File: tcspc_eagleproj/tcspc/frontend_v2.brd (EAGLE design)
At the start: 25.4 x 25.4 mm, 11 parts, among them U1 AD8465, X1 SMA

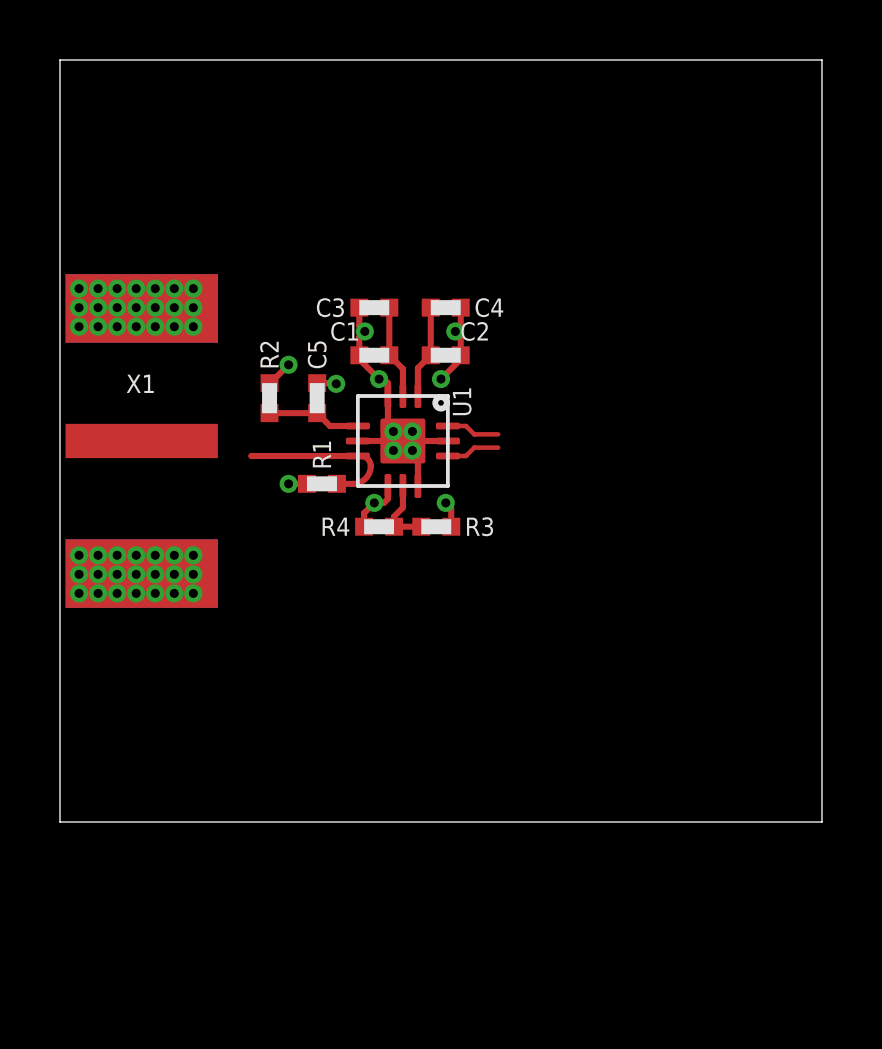
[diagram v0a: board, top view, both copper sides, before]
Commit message: turned the frontend into a useful designblock, ready to be pased all over the tcspc board
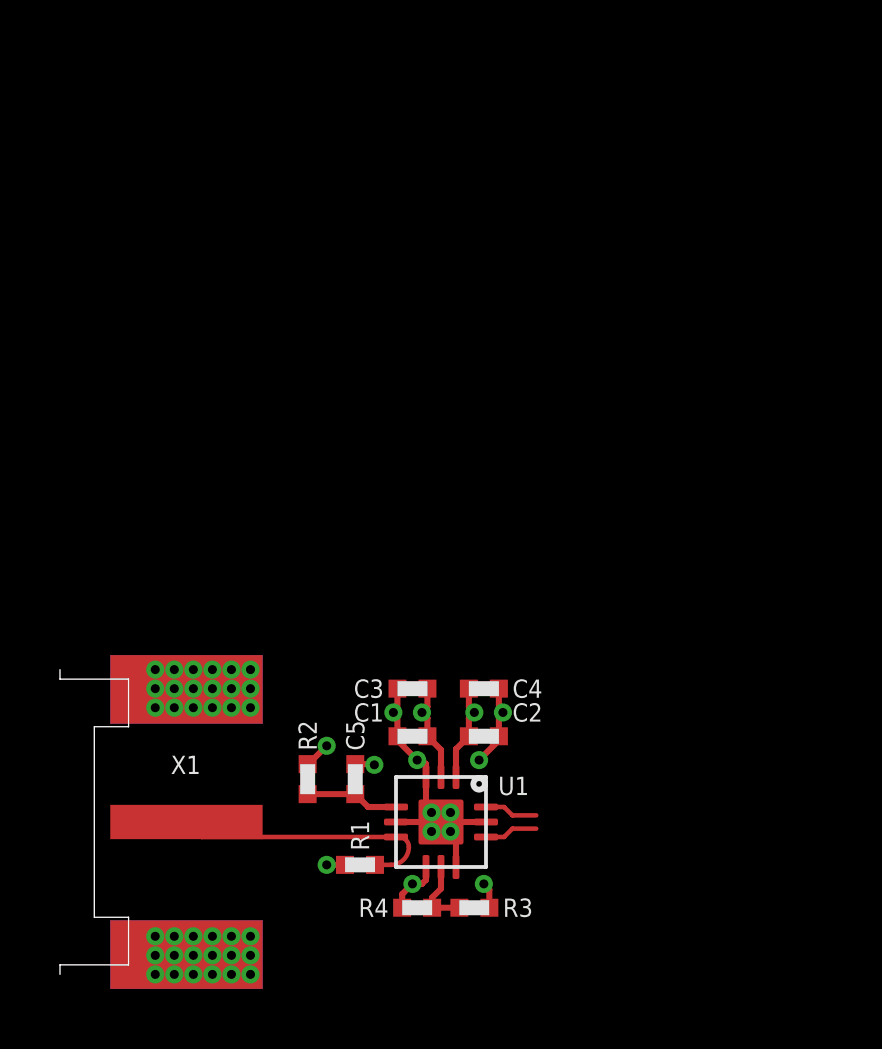
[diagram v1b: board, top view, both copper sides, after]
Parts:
- moved X1 12.8 mm to (1.65, 0.00)
- moved C1 12.8 mm to (11.7, 2.86)
- moved C2 12.8 mm to (14.1, 2.86)
- moved C3 12.8 mm to (11.7, 4.45)
- moved C4 12.8 mm to (14.1, 4.45)
- moved C5 12.8 mm to (9.84, 1.43)
- moved R1 12.8 mm to (10.0, -1.43)
- moved R2 12.8 mm to (8.26, 1.43)
- moved R3 12.8 mm to (13.8, -2.86)
- moved R4 12.8 mm to (11.9, -2.86)
- moved U1 12.8 mm to (12.7, 0.00)
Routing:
- net SIG_IN: track 5.50 -> 9.13 mm
- net PP_P3V3_ANALOG: track 3.13 -> 3.28 mm, vias 0 -> 1
- net PP_P3V3_DIGITAL: track 3.12 -> 3.27 mm, vias 0 -> 1
- net GND: vias 53 -> 47
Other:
- board size 25.4 x 25.4 mm -> 2.3 x 10.2 mm

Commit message: small tweaks to the dbl so that I could start putting four of them onto the main board, and then I did just that.
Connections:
- net LE/HYS renamed CHA_LE/HYS
- net SIG_IN renamed CHA_SIG_IN
- net THRESH renamed CHA_THRESH
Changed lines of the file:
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@@
 <wire x1="14.80223125" y1="-0.5" x2="14.2" y2="-0.5" width="0.1524" layer="1"/>
 </signal>
-<signal name="SIG_IN">
+<signal name="CHA_SIG_IN">
 <contactref element="U1" pad="6"/>
 <contactref element="X1" pad="1"/>
@@
 <wire x1="4.7164" y1="-0.5" x2="4.2164" y2="0" width="0.1524" layer="1"/>
 </signal>
-<signal name="THRESH">
+<signal name="CHA_THRESH">
 <contactref element="U1" pad="4"/>
 <contactref element="C5" pad="1"/>
@@
 <via x="8.89" y="2.54" extent="1-16" drill="0.3"/>
 </signal>
-<signal name="LE/HYS">
+<signal name="CHA_LE/HYS">
 <contactref element="R3" pad="2"/>
 <contactref element="R4" pad="1"/>
